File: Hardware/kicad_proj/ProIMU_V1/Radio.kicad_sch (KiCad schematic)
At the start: 2 parts

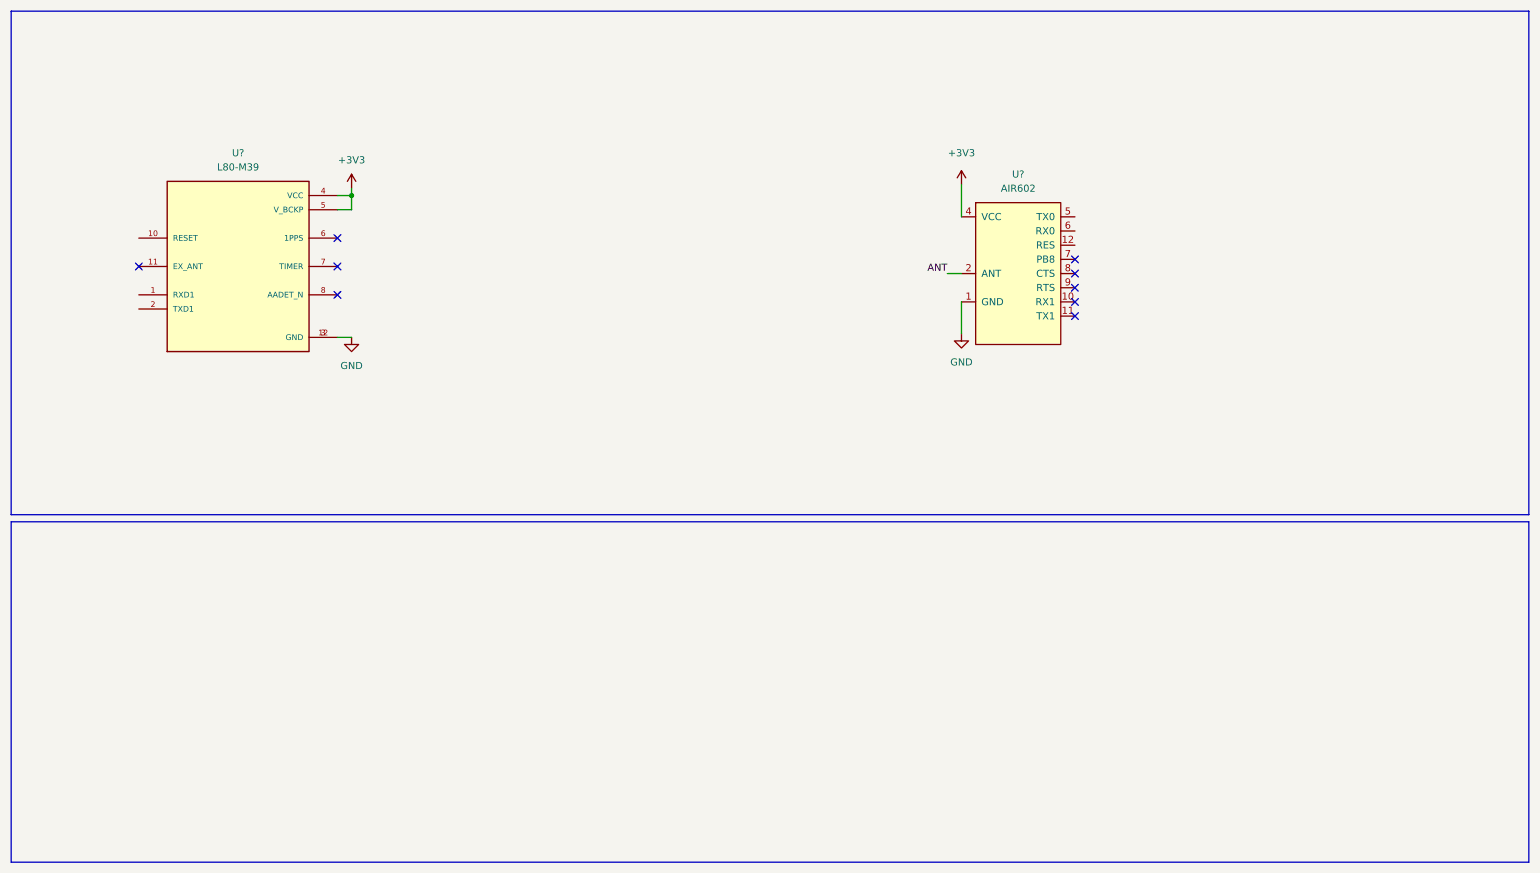
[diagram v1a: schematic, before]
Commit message: Updated schematic and removed redundant schematic
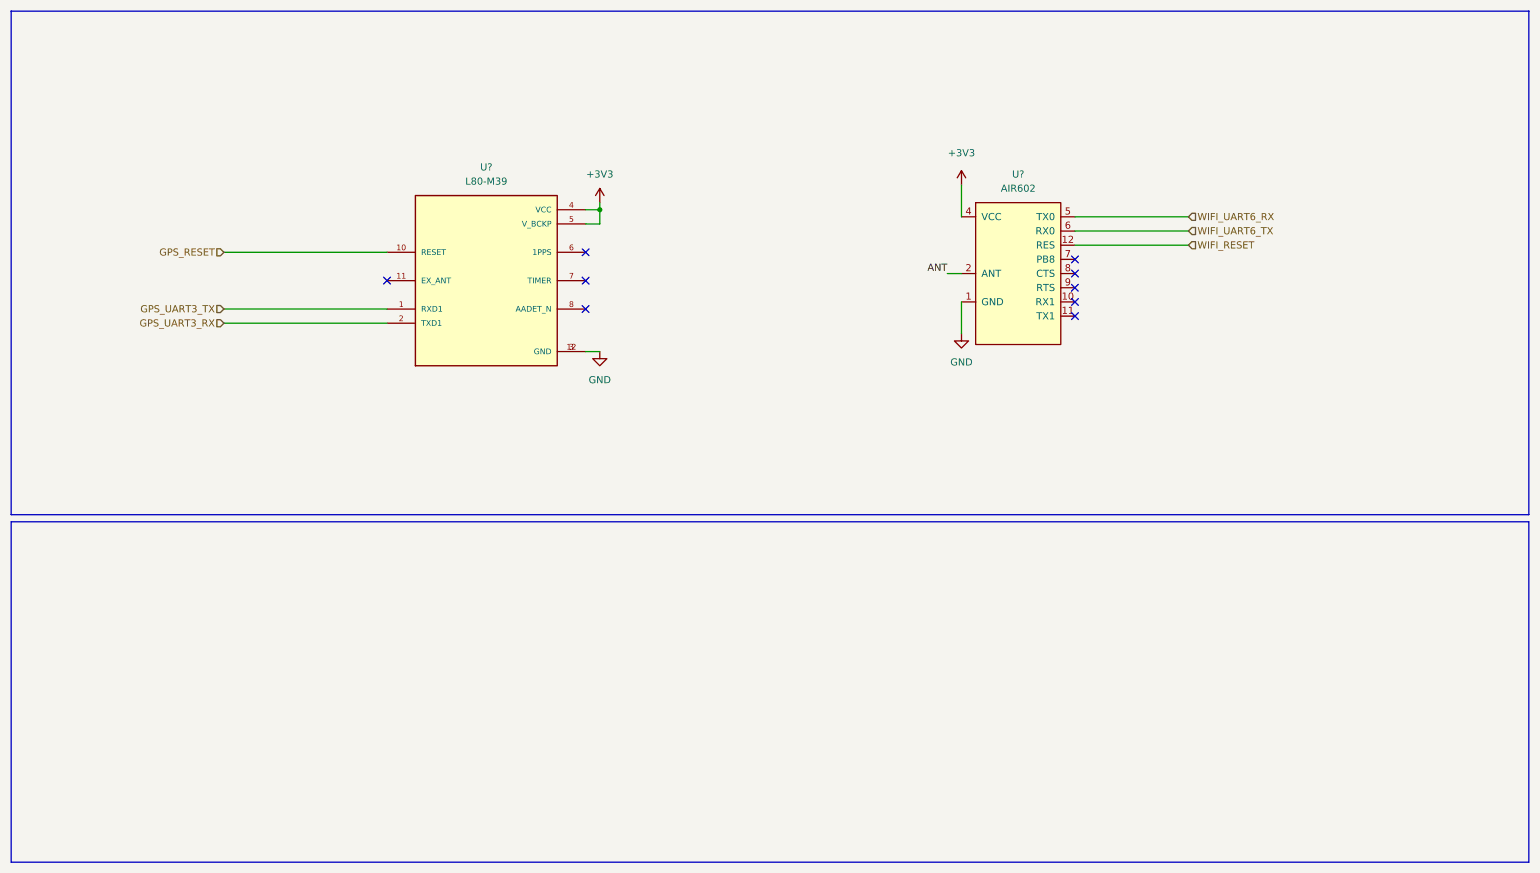
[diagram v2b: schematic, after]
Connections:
- net WIFI_RESET: now reaches U?.12 (RES)
- net WIFI_UART6_RX: now reaches U?.5 (TX0)
- net WIFI_UART6_TX: now reaches U?.6 (RX0)
- net GPS_UART3_TX: now reaches U?.1 (RXD1)
- net GPS_RESET: now reaches U?.10 (RESET)
- net GPS_UART3_RX: now reaches U?.2 (TXD1)
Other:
- moved on the sheet: U?
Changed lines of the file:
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@@
 (kicad_sch (version 20211123) (generator eeschema)
   (paper "A4")
-  (junction (at 73.66 45.72) (diameter 0) (color 0 0 0 0)
+  (junction (at 118.11 48.26) (diameter 0) (color 0 0 0 0)
   )
-  (no_connect (at 35.56 58.42))
-  (no_connect (at 71.12 58.42))
+  (no_connect (at 80.01 60.96))
+  (no_connect (at 115.57 60.96))
   (no_connect (at 203.2 59.69))
-  (no_connect (at 71.12 53.34))
+  (no_connect (at 115.57 55.88))
   (no_connect (at 203.2 62.23))
   (no_connect (at 203.2 64.77))
   (no_connect (at 203.2 57.15))
-  (no_connect (at 71.12 63.5))
+  (no_connect (at 115.57 66.04))
   (no_connect (at 203.2 67.31))
   (polyline (pts (xy 284.48 12.7) (xy 284.48 102.87))
+    (stroke (width 0) (type default) (color 0 0 0 0))
+  )
+  (wire (pts (xy 50.8 55.88) (xy 80.01 55.88))
     (stroke (width 0) (type default) (color 0 0 0 0))
   )
@@
     (stroke (width 0) (type default) (color 0 0 0 0))
   )
-  (wire (pts (xy 71.12 48.26) (xy 73.66 48.26))
+  (wire (pts (xy 50.8 68.58) (xy 80.01 68.58))
+    (stroke (width 0) (type default) (color 0 0 0 0))
+  )
+  (wire (pts (xy 115.57 50.8) (xy 118.11 50.8))
     (stroke (width 0) (type default) (color 0 0 0 0))
   )
@@
     (stroke (width 0) (type default) (color 0 0 0 0))
   )
-  (wire (pts (xy 71.12 71.12) (xy 73.66 71.12))
+  (wire (pts (xy 115.57 73.66) (xy 118.11 73.66))
+    (stroke (width 0) (type default) (color 0 0 0 0))
+  )
+  (wire (pts (xy 203.2 54.61) (xy 223.52 54.61))
     (stroke (width 0) (type default) (color 0 0 0 0))
   )
@@
     (stroke (width 0) (type default) (color 0 0 0 0))
   )
-  (wire (pts (xy 73.66 45.72) (xy 73.66 48.26))
+  (wire (pts (xy 118.11 48.26) (xy 118.11 50.8))
     (stroke (width 0) (type default) (color 0 0 0 0))
   )
-  (wire (pts (xy 71.12 45.72) (xy 73.66 45.72))
+  (wire (pts (xy 115.57 48.26) (xy 118.11 48.26))
     (stroke (width 0) (type default) (color 0 0 0 0))
   )
@@
     (stroke (width 0) (type default) (color 0 0 0 0))
   )
+  (wire (pts (xy 50.8 66.04) (xy 80.01 66.04))
+    (stroke (width 0) (type default) (color 0 0 0 0))
+  )
   (wire (pts (xy 180.34 59.69) (xy 182.88 59.69))
+    (stroke (width 0) (type default) (color 0 0 0 0))
+  )
+  (wire (pts (xy 203.2 49.53) (xy 223.52 49.53))
+    (stroke (width 0) (type default) (color 0 0 0 0))
+  )
+  (wire (pts (xy 203.2 52.07) (xy 223.52 52.07))
     (stroke (width 0) (type default) (color 0 0 0 0))
   )
@@
     (stroke (width 0) (type default) (color 0 0 0 0))
   )
-  (wire (pts (xy 73.66 44.45) (xy 73.66 45.72))
+  (wire (pts (xy 118.11 46.99) (xy 118.11 48.26))
     (stroke (width 0) (type default) (color 0 0 0 0))
   )
@@
   (label "ANT" (at 180.34 59.69 180)
     (effects (font (size 1.27 1.27)) (justify right bottom))
+  )
+  (hierarchical_label "GPS_UART3_TX" (shape input) (at 50.8 66.04 180)
+    (effects (font (size 1.27 1.27)) (justify right))
+  )
+  (hierarchical_label "WIFI_RESET" (shape input) (at 223.52 54.61 0)
+    (effects (font (size 1.27 1.27)) (justify left))
+  )
+  (hierarchical_label "WIFI_UART6_RX" (shape input) (at 223.52 49.53 0)
+    (effects (font (size 1.27 1.27)) (justify left))
+  )
+  (hierarchical_label "GPS_RESET" (shape input) (at 50.8 55.88 180)
+    (effects (font (size 1.27 1.27)) (justify right))
+  )
+  (hierarchical_label "GPS_UART3_RX" (shape input) (at 50.8 68.58 180)
+    (effects (font (size 1.27 1.27)) (justify right))
+  )
+  (hierarchical_label "WIFI_UART6_TX" (shape input) (at 223.52 52.07 0)
+    (effects (font (size 1.27 1.27)) (justify left))
   )
   (symbol (lib_id "air602:AIR602") (at 193.04 57.15 0) (unit 1)
@@
     (pin "9")
   )
-  (symbol (lib_id "power:GND") (at 73.66 71.12 0) (unit 1)
+  (symbol (lib_id "power:GND") (at 118.11 73.66 0) (unit 1)
     (in_bom yes) (on_board yes) (fields_autoplaced)
-    (property "Reference" "#PWR?" (id 0) (at 73.66 77.47 0)
+    (property "Reference" "#PWR?" (id 0) (at 118.11 80.01 0)
       (effects (font (size 1.27 1.27)) hide)
     )
-    (property "Value" "GND" (id 1) (at 73.66 76.2 0))
-    (property "Footprint" "" (id 2) (at 73.66 71.12 0)
+    (property "Value" "GND" (id 1) (at 118.11 78.74 0))
+    (property "Footprint" "" (id 2) (at 118.11 73.66 0)
       (effects (font (size 1.27 1.27)) hide)
     )
-    (property "Datasheet" "" (id 3) (at 73.66 71.12 0)
+    (property "Datasheet" "" (id 3) (at 118.11 73.66 0)
       (effects (font (size 1.27 1.27)) hide)
     )
     (pin "1")
   )
-  (symbol (lib_id "L80-M39:L80-M39") (at 53.34 58.42 0) (unit 1)
+  (symbol (lib_id "L80-M39:L80-M39") (at 97.79 60.96 0) (unit 1)
     (in_bom yes) (on_board yes) (fields_autoplaced)
-    (property "Reference" "U?" (id 0) (at 53.34 38.1 0))
-    (property "Value" "L80-M39" (id 1) (at 53.34 40.64 0))
-    (property "Footprint" "footprints:XCVR_L80-M39" (id 2) (at 53.34 58.42 0)
+    (property "Reference" "U?" (id 0) (at 97.79 40.64 0))
+    (property "Value" "L80-M39" (id 1) (at 97.79 43.18 0))
+    (property "Footprint" "footprints:XCVR_L80-M39" (id 2) (at 97.79 60.96 0)
       (effects (font (size 1.27 1.27)) (justify left bottom) hide)
     )
-    (property "Datasheet" "" (id 3) (at 53.34 58.42 0)
+    (property "Datasheet" "" (id 3) (at 97.79 60.96 0)
       (effects (font (size 1.27 1.27)) (justify left bottom) hide)
     )
-    (property "PACKAGE" "Radial Can  Quectel" (id 4) (at 53.34 58.42 0)
+    (property "PACKAGE" "Radial Can  Quectel" (id 4) (at 97.79 60.96 0)
       (effects (font (size 1.27 1.27)) (justify left bottom) hide)
     )
-    (property "AVAILABILITY" "Unavailable" (id 5) (at 53.34 58.42 0)
+    (property "AVAILABILITY" "Unavailable" (id 5) (at 97.79 60.96 0)
       (effects (font (size 1.27 1.27)) (justify left bottom) hide)
     )
-    (property "PRICE" "None" (id 6) (at 53.34 58.42 0)
+    (property "PRICE" "None" (id 6) (at 97.79 60.96 0)
       (effects (font (size 1.27 1.27)) (justify left bottom) hide)
     )
-    (property "MP" "L80" (id 7) (at 53.34 58.42 0)
+    (property "MP" "L80" (id 7) (at 97.79 60.96 0)
       (effects (font (size 1.27 1.27)) (justify left bottom) hide)
     )
-    (property "DESCRIPTION" "L80 is an ultra compact GPS POT _Patch on Top_ module with an embedded 15.0mm × 15.0mm × 4.0mm patch antenna." (id 8) (at 53.34 58.42 0)
+    (property "DESCRIPTION" "L80 is an ultra compact GPS POT _Patch on Top_ module with an embedded 15.0mm × 15.0mm × 4.0mm patch antenna." (id 8) (at 97.79 60.96 0)
       (effects (font (size 1.27 1.27)) (justify left bottom) hide)
     )
-    (property "MF" "Quectel" (id 9) (at 53.34 58.42 0)
+    (property "MF" "Quectel" (id 9) (at 97.79 60.96 0)
       (effects (font (size 1.27 1.27)) (justify left bottom) hide)
     )
@@
     (pin "8")
   )
-  (symbol (lib_id "power:+3V3") (at 73.66 44.45 0) (unit 1)
+  (symbol (lib_id "power:+3V3") (at 118.11 46.99 0) (unit 1)
     (in_bom yes) (on_board yes) (fields_autoplaced)
-    (property "Reference" "#PWR?" (id 0) (at 73.66 48.26 0)
+    (property "Reference" "#PWR?" (id 0) (at 118.11 50.8 0)
       (effects (font (size 1.27 1.27)) hide)
     )
-    (property "Value" "+3V3" (id 1) (at 73.66 39.37 0))
-    (property "Footprint" "" (id 2) (at 73.66 44.45 0)
+    (property "Value" "+3V3" (id 1) (at 118.11 41.91 0))
+    (property "Footprint" "" (id 2) (at 118.11 46.99 0)
       (effects (font (size 1.27 1.27)) hide)
     )
-    (property "Datasheet" "" (id 3) (at 73.66 44.45 0)
+    (property "Datasheet" "" (id 3) (at 118.11 46.99 0)
       (effects (font (size 1.27 1.27)) hide)
     )

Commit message: Updated Schematic and Layout
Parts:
- gave numbers to parts that had none: 2
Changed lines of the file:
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@@
   (symbol (lib_id "air602:AIR602") (at 193.04 57.15 0) (unit 1)
     (in_bom yes) (on_board yes) (fields_autoplaced)
-    (property "Reference" "U?" (id 0) (at 193.04 41.91 0))
+    (property "Reference" "U4" (id 0) (at 193.04 41.91 0))
     (property "Value" "AIR602" (id 1) (at 193.04 44.45 0))
     (property "Footprint" "footprints:AIR602" (id 2) (at 193.04 57.15 0)
@@
   (symbol (lib_id "power:GND") (at 118.11 73.66 0) (unit 1)
     (in_bom yes) (on_board yes) (fields_autoplaced)
-    (property "Reference" "#PWR?" (id 0) (at 118.11 80.01 0)
+    (property "Reference" "#PWR0122" (id 0) (at 118.11 80.01 0)
       (effects (font (size 1.27 1.27)) hide)
     )
@@
   (symbol (lib_id "L80-M39:L80-M39") (at 97.79 60.96 0) (unit 1)
     (in_bom yes) (on_board yes) (fields_autoplaced)
-    (property "Reference" "U?" (id 0) (at 97.79 40.64 0))
+    (property "Reference" "U3" (id 0) (at 97.79 40.64 0))
     (property "Value" "L80-M39" (id 1) (at 97.79 43.18 0))
     (property "Footprint" "footprints:XCVR_L80-M39" (id 2) (at 97.79 60.96 0)
@@
   (symbol (lib_id "power:+3V3") (at 118.11 46.99 0) (unit 1)
     (in_bom yes) (on_board yes) (fields_autoplaced)
-    (property "Reference" "#PWR?" (id 0) (at 118.11 50.8 0)
+    (property "Reference" "#PWR0121" (id 0) (at 118.11 50.8 0)
       (effects (font (size 1.27 1.27)) hide)
     )
@@
   (symbol (lib_id "power:+3V3") (at 182.88 43.815 0) (unit 1)
     (in_bom yes) (on_board yes) (fields_autoplaced)
-    (property "Reference" "#PWR?" (id 0) (at 182.88 47.625 0)
+    (property "Reference" "#PWR0124" (id 0) (at 182.88 47.625 0)
       (effects (font (size 1.27 1.27)) hide)
     )
@@
   (symbol (lib_id "power:GND") (at 182.88 70.485 0) (unit 1)
     (in_bom yes) (on_board yes) (fields_autoplaced)
-    (property "Reference" "#PWR?" (id 0) (at 182.88 76.835 0)
+    (property "Reference" "#PWR0123" (id 0) (at 182.88 76.835 0)
       (effects (font (size 1.27 1.27)) hide)
     )

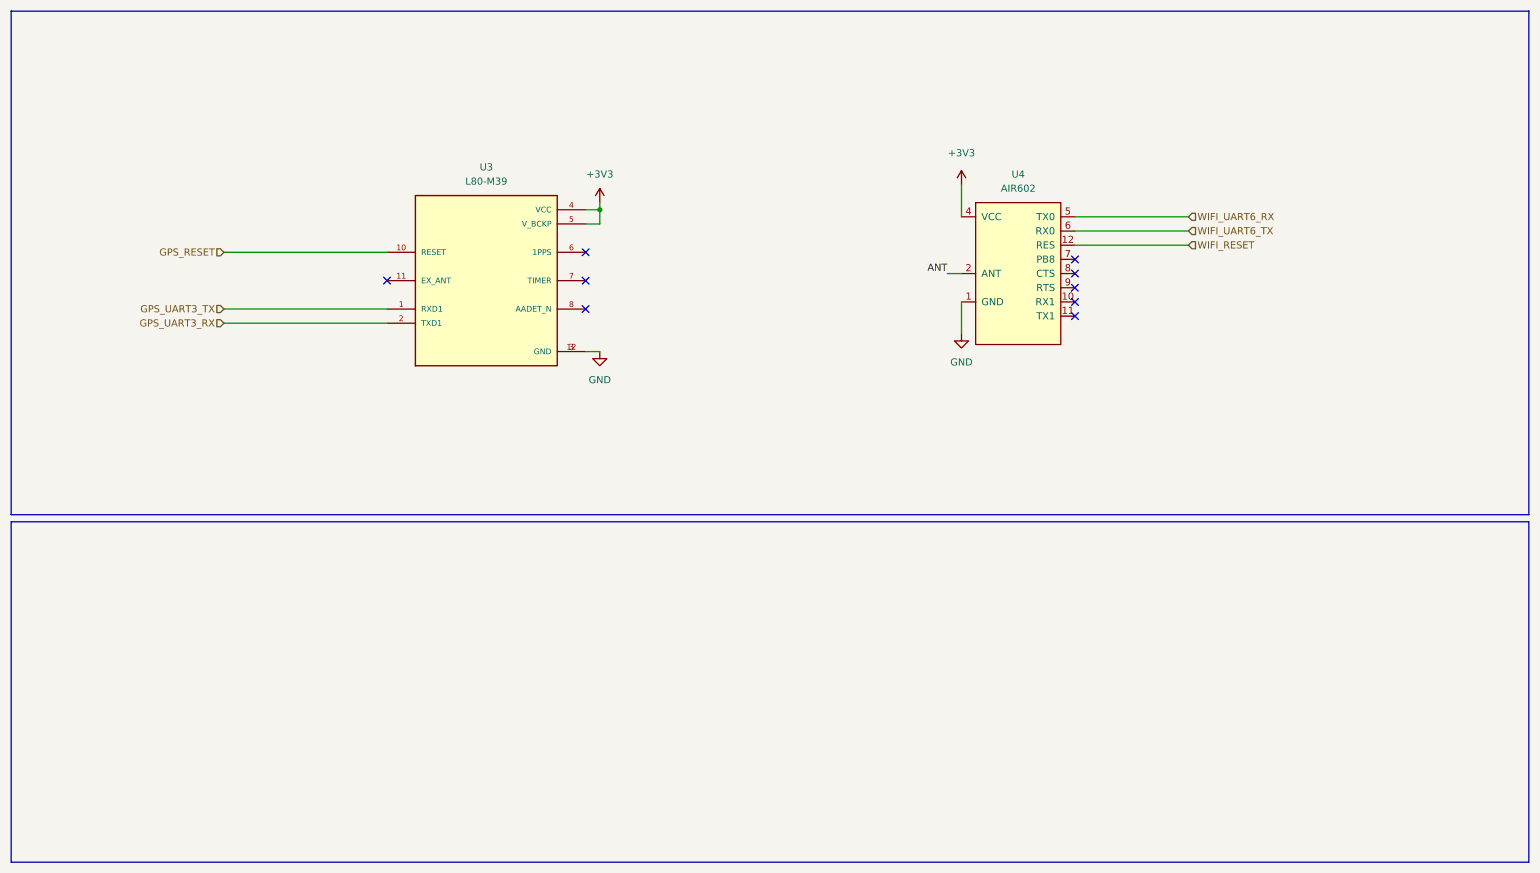
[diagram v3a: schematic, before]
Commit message: Added BNO055 to design and removed MPU9250.
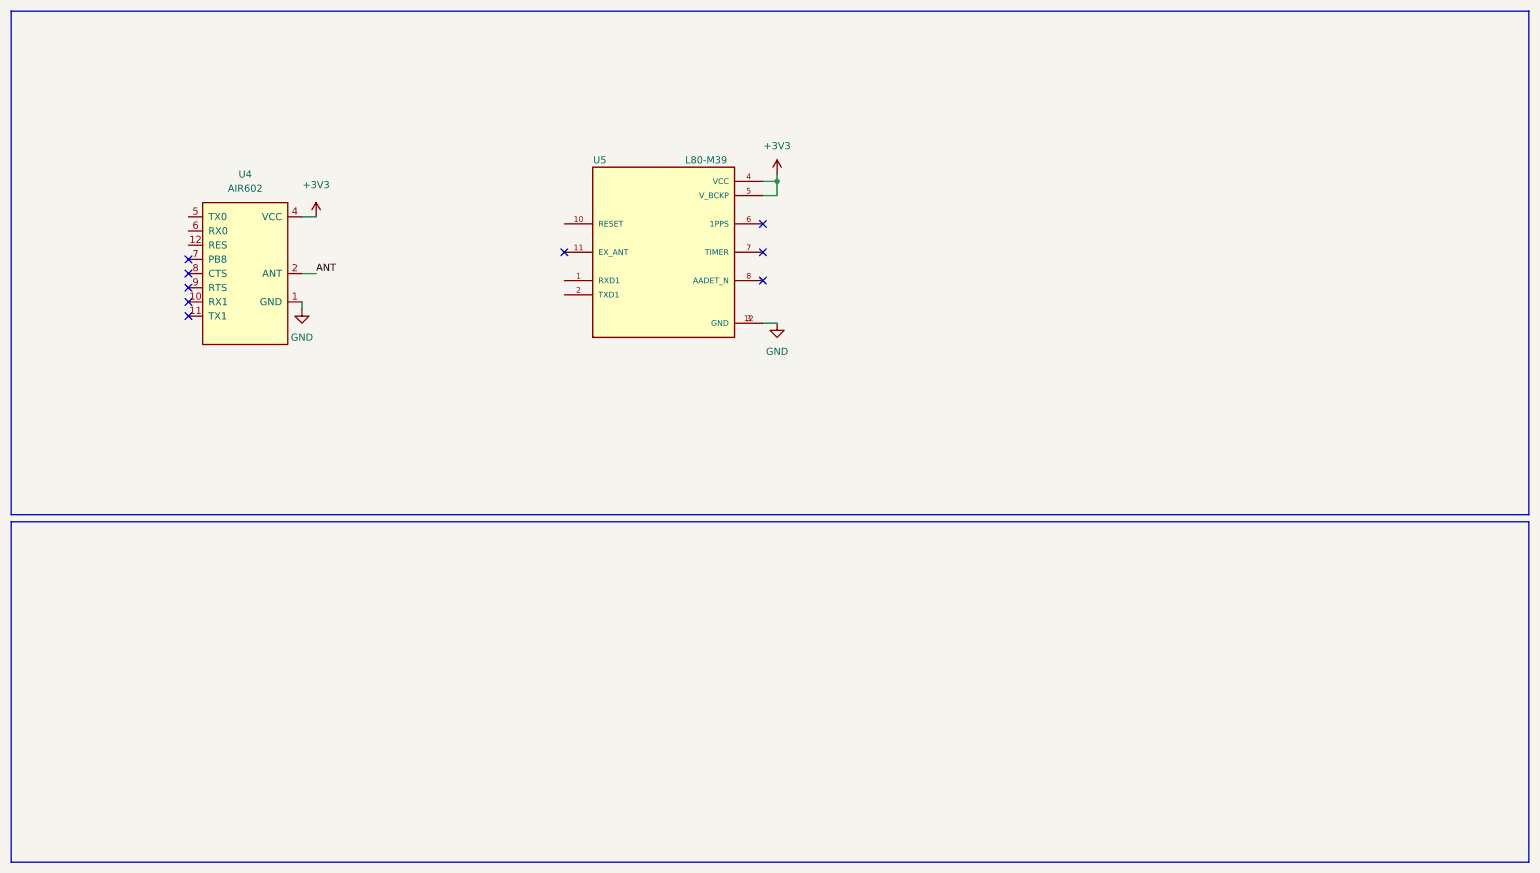
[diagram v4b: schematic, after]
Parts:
- removed U3: L80-M39, footprints:XCVR_L80-M39, symbol L80-M39:L80-M39
- added U5: L80-M39, footprints:XCVR_L80-M39, symbol L80-M39:L80-M39
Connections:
- net +3V3: now also U5.4 (VCC), U5.5 (V_BCKP)
- net GND: now also U5.12 (GND), U5.3 (GND)
- net WIFI_RESET: no longer names the net of U4.12 (RES)
- net WIFI_UART6_RX: no longer names the net of U4.5 (TX0)
- net WIFI_UART6_TX: no longer names the net of U4.6 (RX0)
